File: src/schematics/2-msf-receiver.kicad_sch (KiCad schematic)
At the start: 68 parts, among them U201 TPS7A2040PDQNR, U202 TPS7A2036PDBVR, U203 MCP6499, U204 MCP6499, U205 74HC595BQ

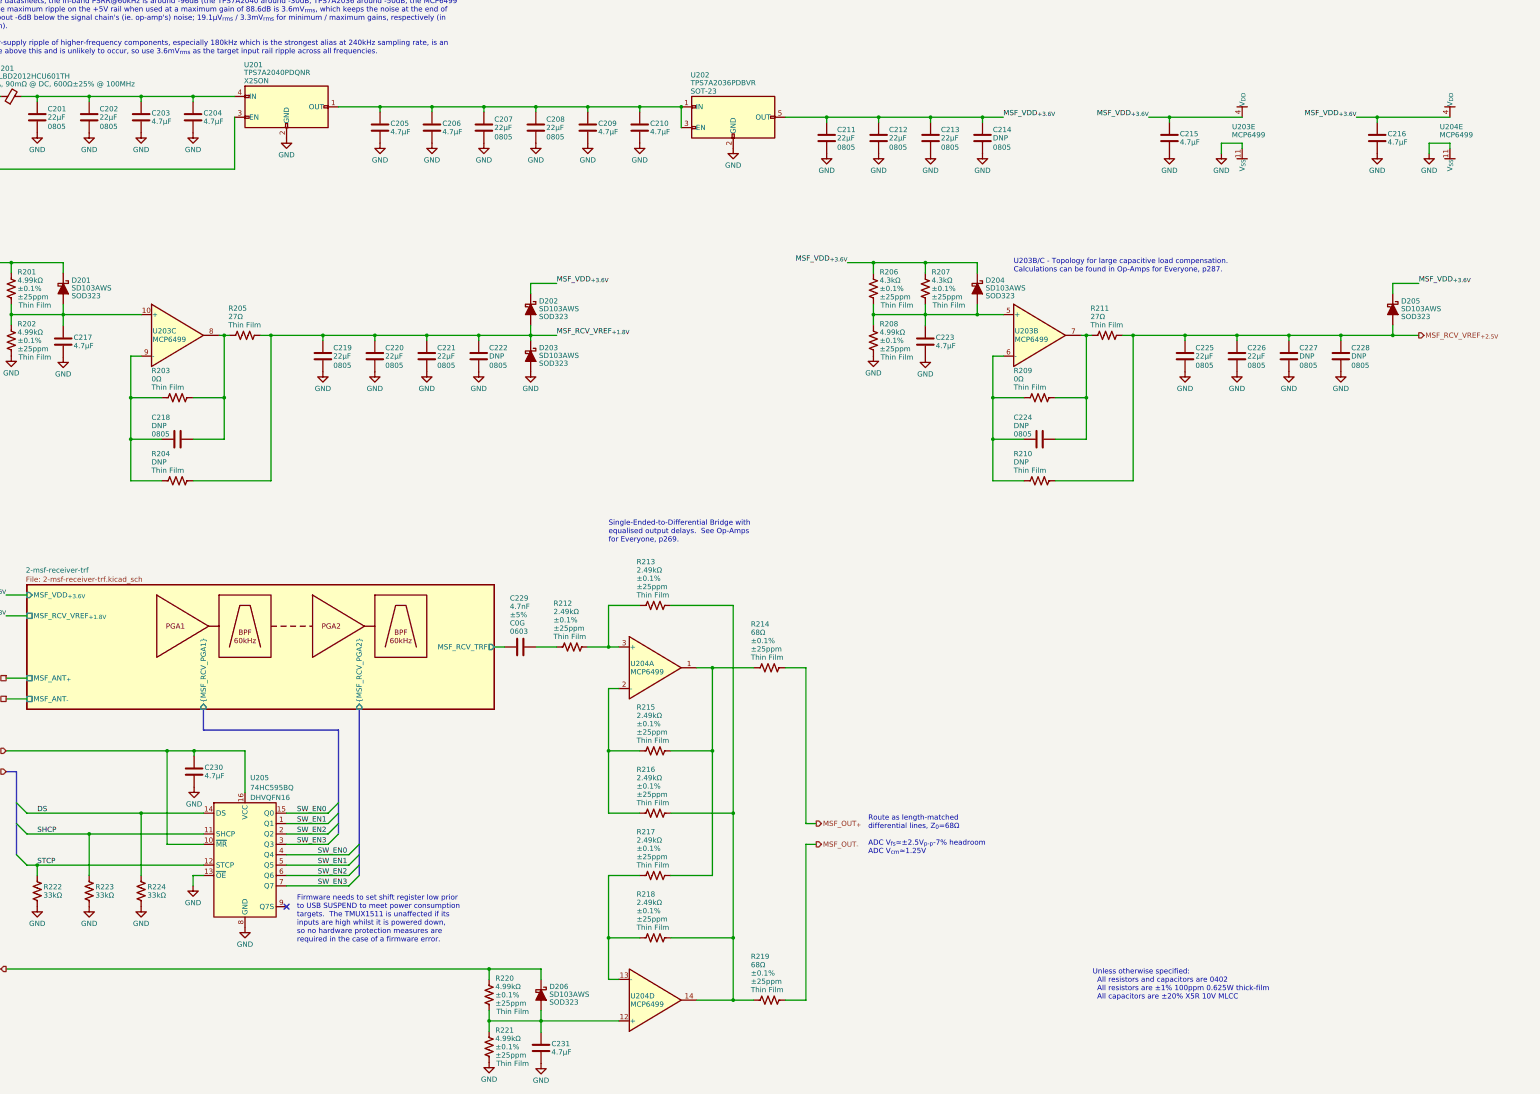
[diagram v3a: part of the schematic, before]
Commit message: Added another bypass capacitor.
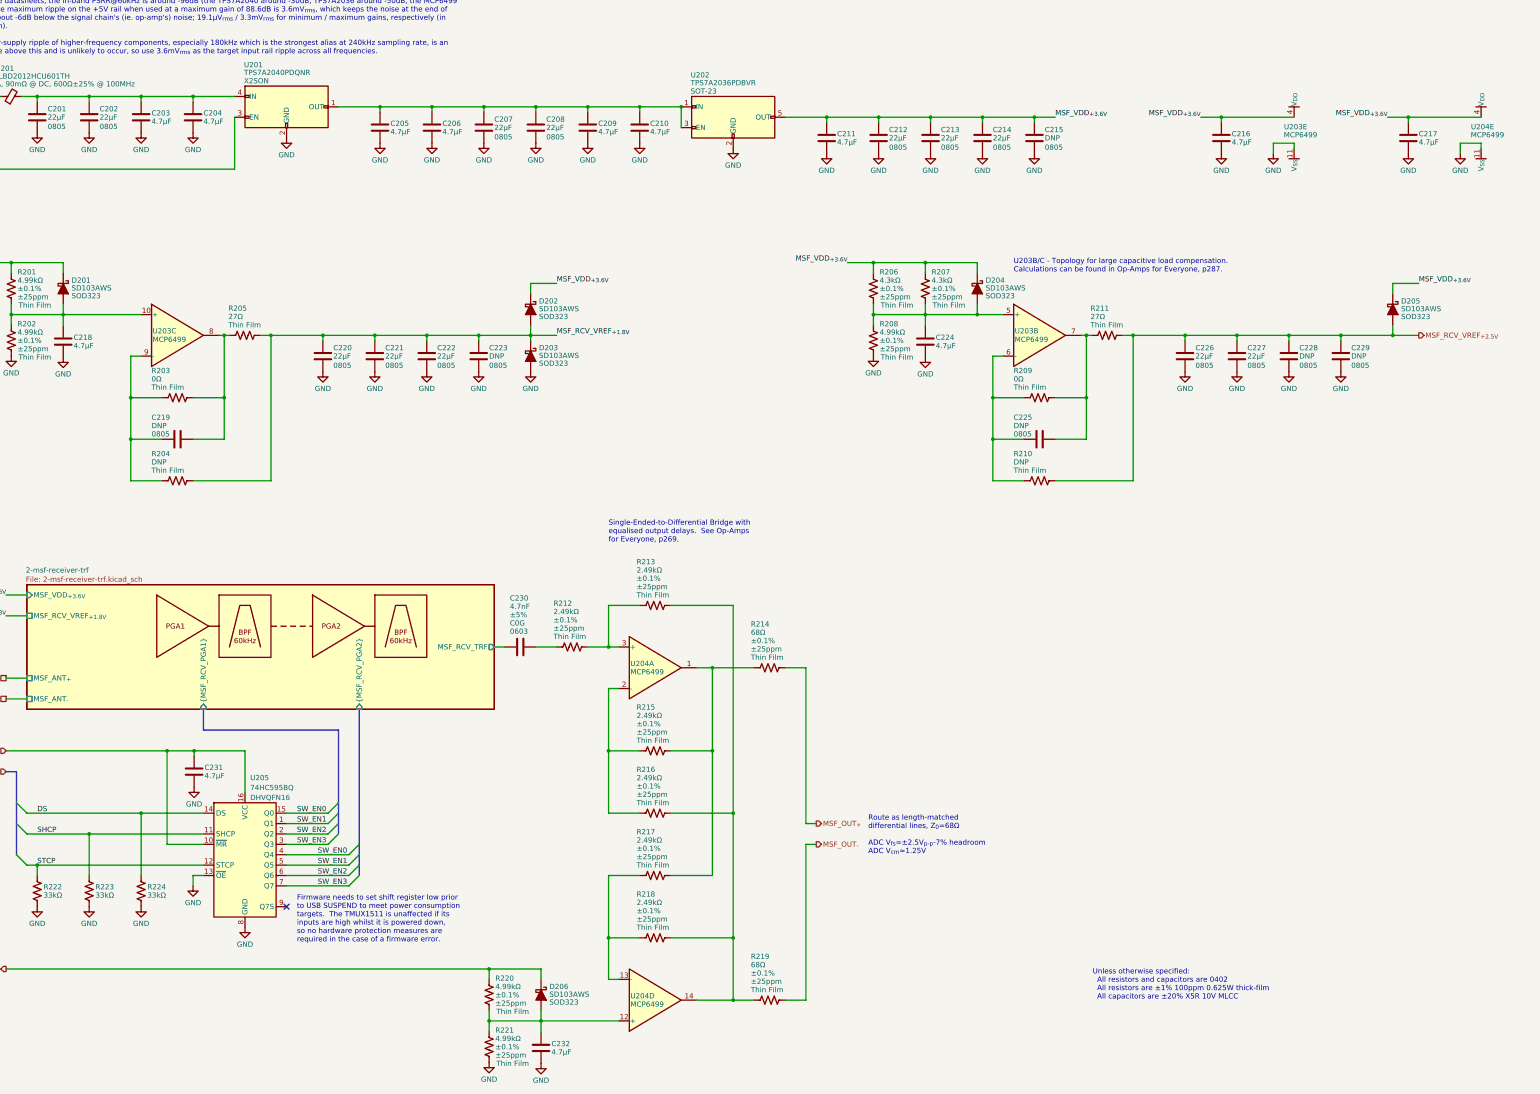
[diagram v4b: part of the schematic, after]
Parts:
- added C211: 4.7μF, restall-generic-capacitors:unpolarised-nominal-0402-1005, symbol restall-generic-capacitors:capacitor-unpolarised
- renumbered C211 to C212, C212 to C213, C213 to C214, C214 to C215, C215 to C216, C216 to C217, C217 to C218, C218 to C219, C219 to C220, C220 to C221, C221 to C222, C222 to C223, C223 to C224, C224 to C225, C225 to C226, C226 to C227, C227 to C228, C228 to C229, C229 to C230, C230 to C231, C231 to C232
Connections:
- net GND: now also C211.2
- net MSF_VDD_{+3.6V}: now also C211.1
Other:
- moved on the sheet: C212, C213, C214, C215, C216, C217, U203E, U204E

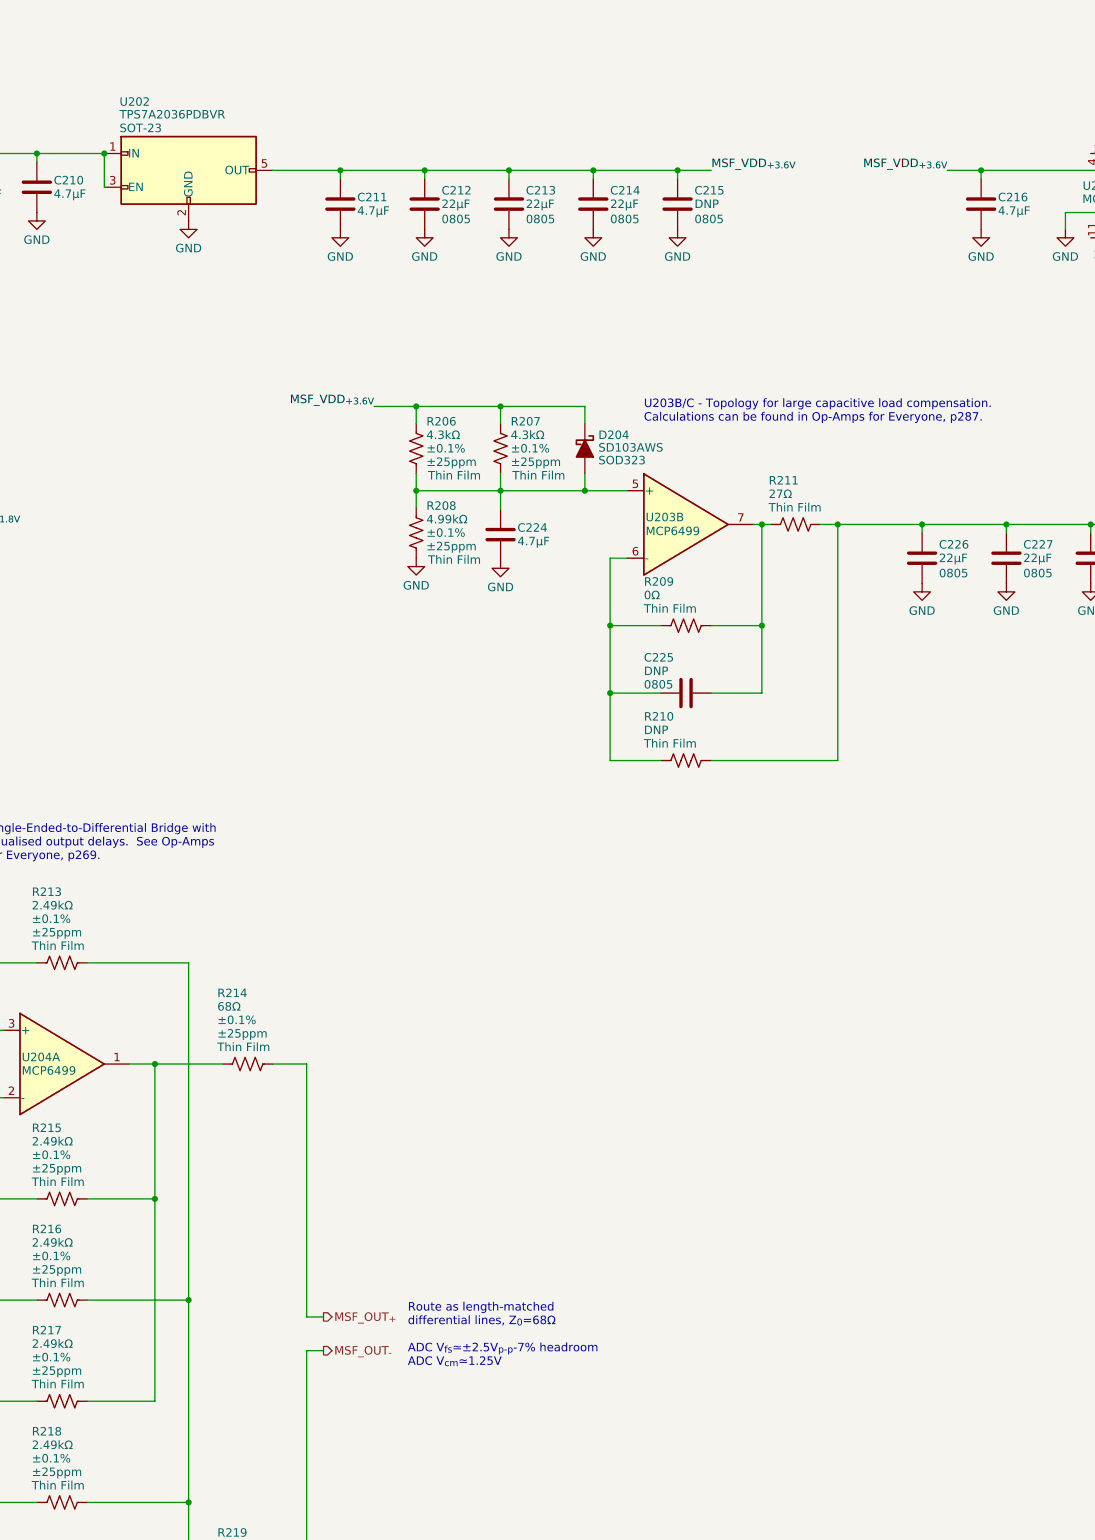
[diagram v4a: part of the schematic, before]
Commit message: Added a note about ADC injection currents.
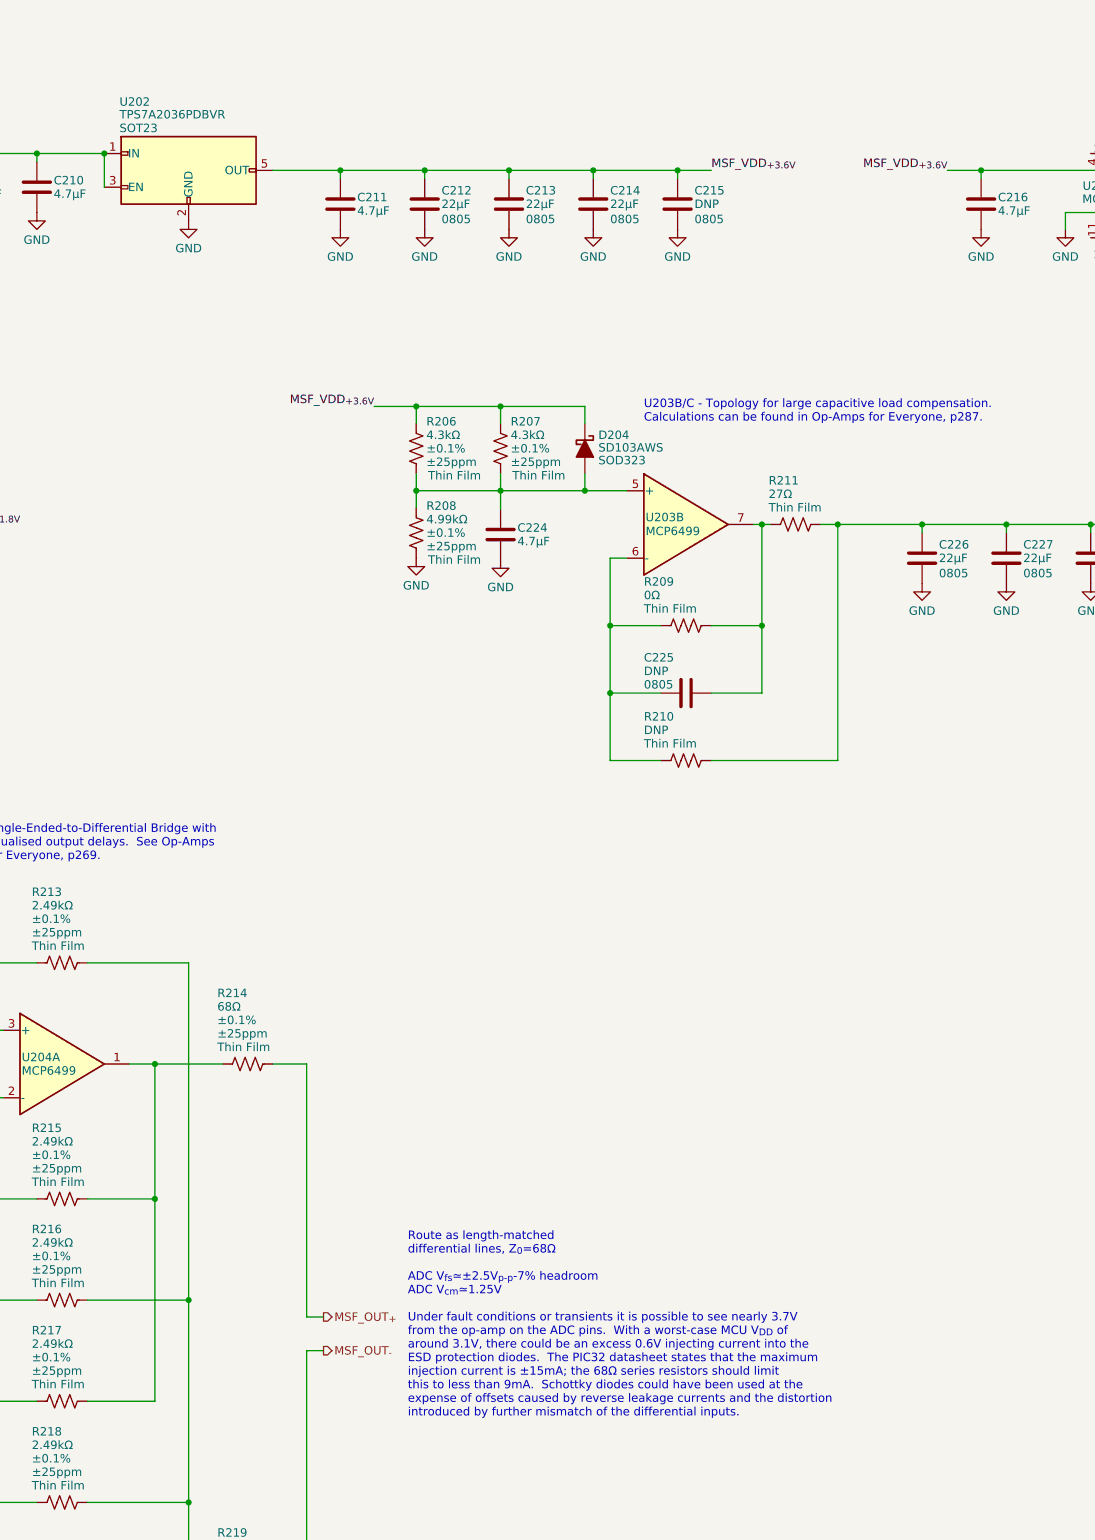
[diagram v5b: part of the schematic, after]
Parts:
- U202: Package SOT-23 -> SOT23
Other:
- note added: "Route as length-matched differential lines, Z_{0}=68Ω ADC V_{fs}≃±2.5V_{p-p}-7% headroom ADC V_{cm}≃1.25V Under fault conditions or transients it is possible to see nearly 3.7V from the op-amp on the ADC pins. With a worst-case MCU V_{DD} of around 3.1V, there could be an excess 0.6V injecting current into the ESD protection diodes. The PIC32 datasheet states that the maximum injection current is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"
- note removed: "Route as length-matched differential lines, Z_{0}=68Ω ADC V_{fs}≃±2.5V_{p-p}-7% headroom ADC V_{cm}≃1.25V"
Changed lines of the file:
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@@
     (effects (font (size 1.27 1.27)) (justify left bottom))
   )
-  (text "Route as length-matched\ndifferential lines, Z_{0}=68Ω\n\nADC V_{fs}≃±2.5V_{p-p}-7% headroom\nADC V_{cm}≃1.25V"
-    (at 246.38 226.06 0)
+  (text "Route as length-matched\ndifferential lines, Z_{0}=68Ω\n\nADC V_{fs}≃±2.5V_{p-p}-7% headroom\nADC V_{cm}≃1.25V\n\nUnder fault conditions or transients it is possible to see nearly 3.7V\nfrom the op-amp on the ADC pins.  With a worst-case MCU V_{DD} of\naround 3.1V, there could be an excess 0.6V injecting current into the\nESD protection diodes.  The PIC32 datasheet states that the maximum\ninjection current is ±15mA; the 68Ω series resistors should limit\nthis to less than 9mA.  Schottky diodes could have been used at the\nexpense of offsets caused by reverse leakage currents and the distortion\nintroduced by further mismatch of the differential inputs."
+    (at 246.38 233.68 0)
     (effects (font (size 1.27 1.27)) (justify left bottom))
   )
@@
       (effects (font (size 1.27 1.27)) (justify left) hide)
     )
-    (property "Package" "SOT-23" (at 202.946 39.37 0)
-      (effects (font (size 1.27 1.27)) (justify left))
-    )
+    (property "Package" "SOT23" (at 202.946 39.37 0)
+      (effects (font (size 1.27 1.27)) (justify left))
+    )

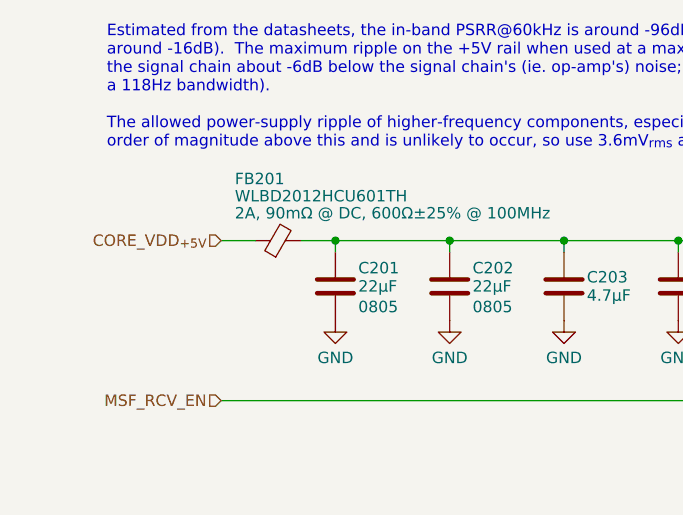
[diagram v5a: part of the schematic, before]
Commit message: Drew the schematic for the TFT driver.
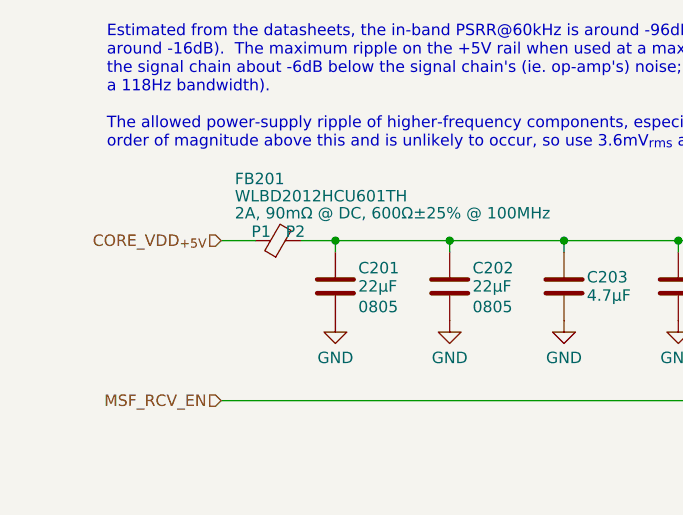
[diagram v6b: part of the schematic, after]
